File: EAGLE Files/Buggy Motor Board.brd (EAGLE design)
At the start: 100 x 80 mm, 53 parts, among them CON0 M025MM, CON1 M025MM, IC4 4050D, IC5 LP298XS, U1 MCP2551, X1 MICROSD, X2 5566-24, X3 5566-24, Y2 16MHZ

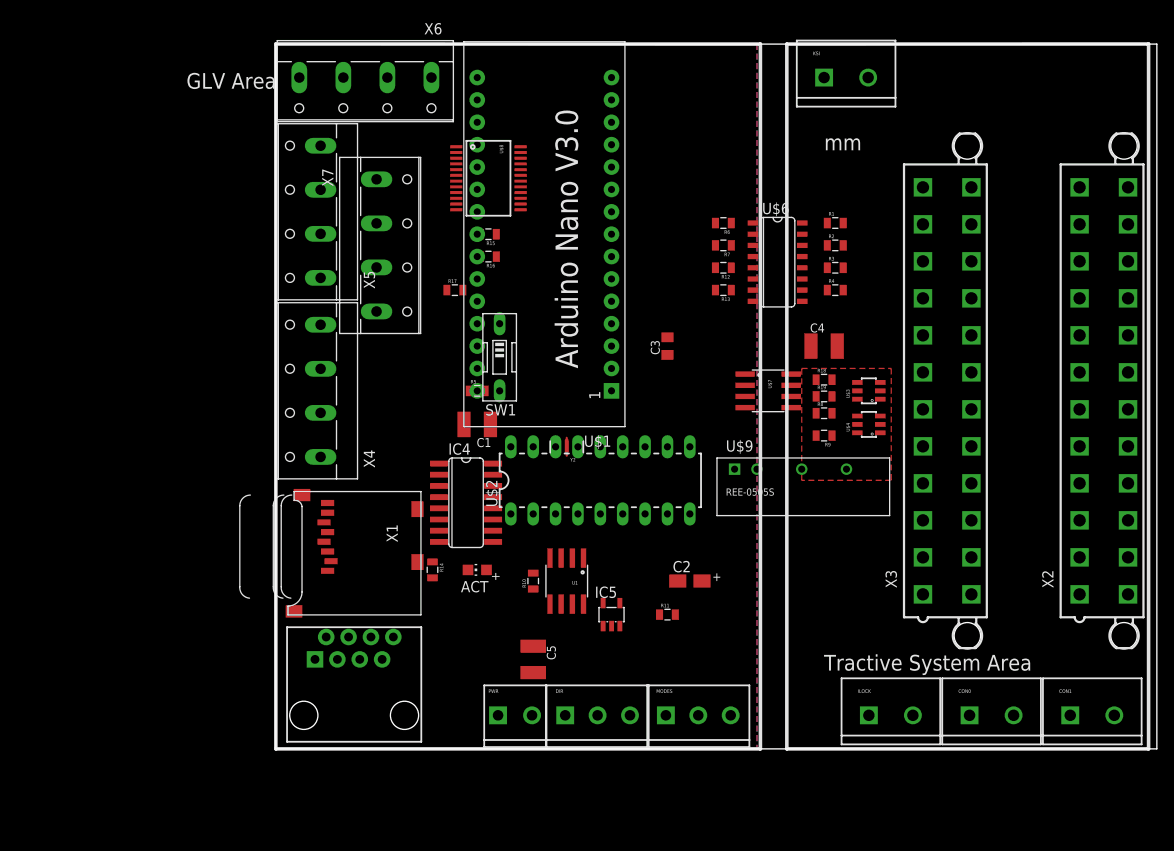
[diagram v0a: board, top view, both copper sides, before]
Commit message: Replace Nano with Teensy 3.1
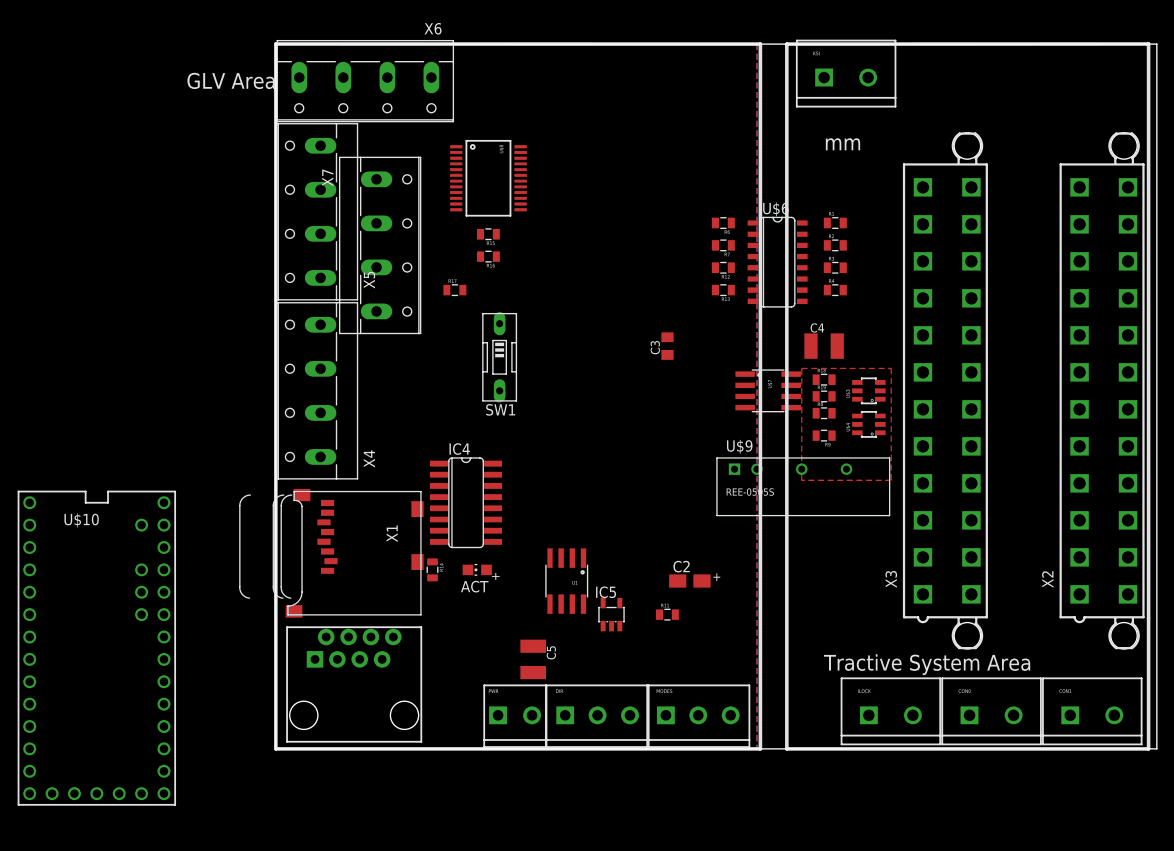
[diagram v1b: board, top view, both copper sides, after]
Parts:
- removed C1: (no value), rcl:C1210K
- removed R10, R5: (no value), SparkFun-Resistors:0805
- removed U$1: ARDUINO_NANO, Wetmelon-Boards:ARDUINO_NANO
- removed U$2: MCP2515, Wetmelon-DigitalIC:DIL18
- removed Y2: 16MHZ, SparkFun-FreqCtrl:RESONATOR-SMD
- added U$10: TEENSY_3.1+4, Teensy_3_Series_Board_v1.0:TEENSY_3.1+4
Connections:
- removed net CAN_CS: U$1.SS*, U$2.12
- removed net INT0: U$1.D2, U$2.16
- removed net INT1: U$1.D3*
- removed net N$1: U$1.3V3
- removed net N$10: U$2.17
- removed net N$11: U$2.18
- removed net N$14: U$2.7, Y2.1
- removed net N$2: U$2.8, Y2.3
- removed net N$23: R5.1, U$1.RES, U$1.RES@1
- removed net N$28: U$1.D8
- removed net N$3: R10.2, U$2.11
- removed net N$4: U$2.3
- removed net N$5: U$2.4
- removed net N$6: U$2.5
- removed net N$9: U$2.6
- new net +3.3V: U1.3
- new net 3.3V: U$10.3.3V, U$10.3.3V1
- new net AREF: U$10.AREF
- new net VBAT: U$10.VBAT
- new net VIN: U$10.VIN
- new net VUSB: U$10.VUSB
- net +12V: no longer C1.1, R5.2, U$1.VIN
- net +5V: no longer R10.1, U$1.+5V, U$2.10, U1.3
- net AGND: now also U$10.AGND
- net AMUX0: no longer U$1.A0
- net AMUX1: no longer U$1.A1
- net AMUX2: no longer U$1.A2
- net AMUX3: no longer U$1.A3
- net AMUX_IN: no longer U$1.A6
- net GND: now also U$10.GND, U$10.GND1; no longer C1.2, U$1.GND, U$1.GND@1, U$2.9, Y2.2
- net MISO: now also U$10.12; no longer U$1.MISO, U$2.13
- net MOSI: now also U$10.11; no longer U$1.MOSI*, U$2.14
- net RXCAN: now also U$10.4; no longer U$2.2
- net SCK: now also U$10.13; no longer U$1.SCK, U$2.15
- net SCL: now also U$10.19/A5; no longer U$1.SCL/A5
- net SDA: now also U$10.18/A4; no longer U$1.SDA/A4
- net SD_CS: no longer U$1.D9*
- net TXCAN: now also U$10.3; no longer U$2.1

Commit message: Add microfit connector
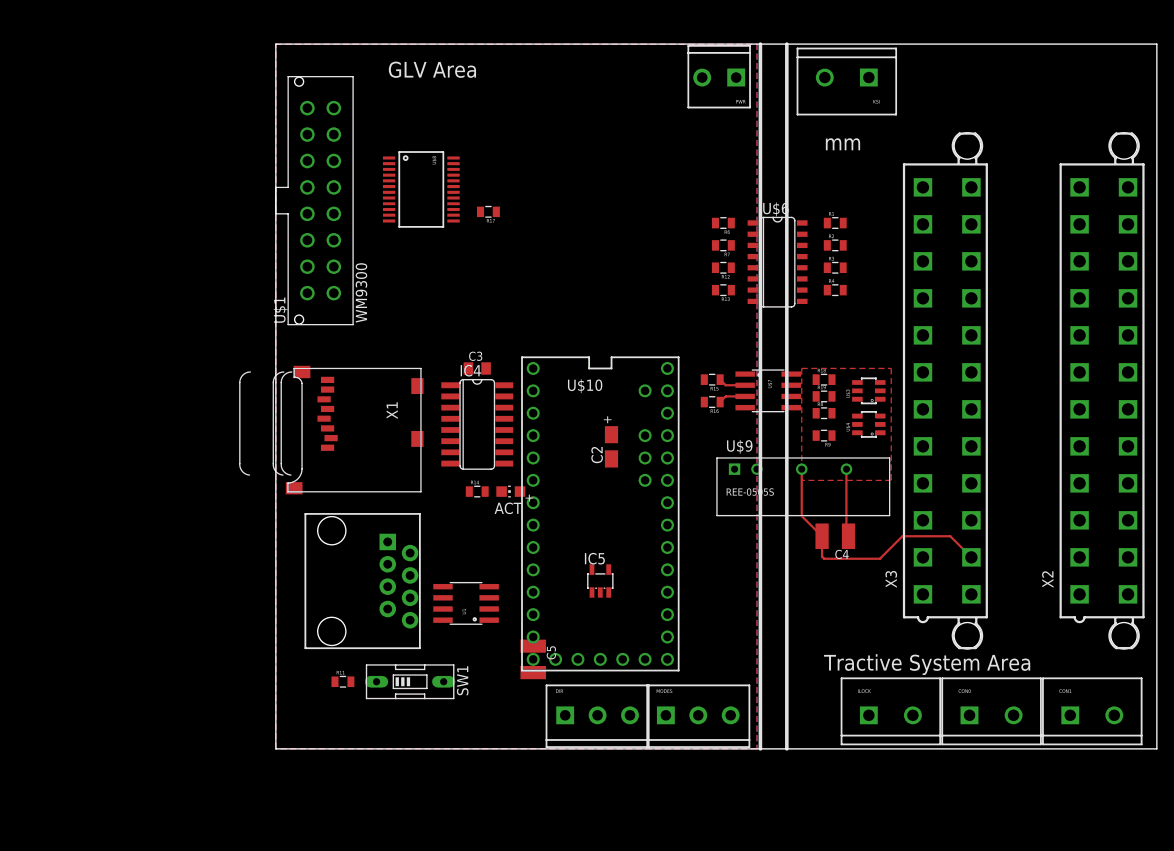
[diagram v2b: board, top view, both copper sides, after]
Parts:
- removed X4, X5, X6, X7: (no value), con-wago-500:W237-4
- added U$1: WM9300, Wetmelon-Connectors:WM9300
- moved PWR 77.1 mm to (52.1, 76.2), turned to 180 degrees
- moved U$10 59.1 mm to (36.8, 25.4)
- moved SW1 38.2 mm to (15.2, 7.62), turned to 270 degrees
- moved R11 37.6 mm to (7.62, 7.62)
- moved R15 30.3 mm to (49.5, 41.9)
- moved R16 30.3 mm to (49.5, 39.4)
- moved C3 21.7 mm to (22.9, 43.2), turned to 0 degrees
- moved C4 21.6 mm to (63.5, 24.1), turned to 180 degrees
- moved C2 17.6 mm to (38.1, 34.3), turned to 90 degrees
- moved U$5 15.5 mm to (6.35, 19.1), turned to 270 degrees
- moved X1 14.0 mm to (16.5, 43.2)
- moved U1 11.7 mm to (21.6, 16.5), turned to 90 degrees
- moved R14 10.2 mm to (22.9, 29.2), turned to 0 degrees
- moved ACT 9.67 mm to (26.7, 29.2)
- moved R17 9.67 mm to (24.1, 61.0), turned to 180 degrees
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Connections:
- removed net CLK: IC4.3, IC4.9
- new net N$1: U$10.2
- new net N$3: U$10.6
- new net N$4: U$10.7
- new net N$5: U$10.8
- net +5V: no longer U$8.24
- net AGND: now also KSI.2; no longer KSI.1
- net AMUX_IN: now also U$10.14/A0
- net CHAN0: now also U$1.8; no longer X4.1
- net CHAN1: now also U$1.7; no longer X4.2
- net CHAN10: now also U$1.11; no longer X6.3
- net CHAN11: now also U$1.12; no longer X6.4
- net CHAN12: now also U$1.13; no longer X7.1
- net CHAN13: now also U$1.14; no longer X7.2
- net CHAN14: now also U$1.15; no longer X7.3
- net CHAN15: now also U$1.16; no longer X7.4
- net CHAN2: now also U$1.6; no longer X4.3
- net CHAN3: now also U$1.5; no longer X4.4
- net CHAN4: now also U$1.4; no longer X5.1
- net CHAN5: now also U$1.3; no longer X5.2
- net CHAN6: now also U$1.2; no longer X5.3
- net CHAN7: now also U$1.1; no longer X5.4
- net CHAN8: now also U$1.9; no longer X6.1
- net CHAN9: now also U$1.10; no longer X6.2
- net KSI: now also KSI.1; no longer KSI.2
- net SCK: now also IC4.3, IC4.9
- net SD_CS: now also U$10.5
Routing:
- net GND1: track 0.00 -> 30.0 mm
- net +5V/1: track 0.00 -> 7.72 mm
- net SCL: track 0.00 -> 3.10 mm
- net SDA: track 0.00 -> 3.10 mm
- added copper zone on layer 1, net GND
- removed copper zone on layer 1, net +5V

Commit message: Tweaks
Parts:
- moved U$10 35.6 mm to (36.8, 61.0)
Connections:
- removed net 3.3V: U$10.3.3V, U$10.3.3V1
- removed net AREF: U$10.AREF
- removed net N$3: U$10.6
- removed net N$4: U$10.7
- removed net N$5: U$10.8
- net +3V3: now also R15.2, R16.2, U$10.3.3V, U$10.3.3V1, U$10.AREF, U$7.1
- net +5V: now also U$8.24; no longer R15.2, R16.2, U$7.1
- net AGND: no longer KSI.2, U$6.11, U$6.13, U$6.15, U$6.9
- net AMUX0: now also U$10.6
- net AMUX1: now also U$10.7
- net AMUX2: now also U$10.8
- net AMUX3: now also U$10.9
- net GND1: now also KSI.2, U$6.11, U$6.13, U$6.15, U$6.9
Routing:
- net AMUX1: track 0.00 -> 17.2 mm, vias 0 -> 1
- net AMUX0: track 0.00 -> 16.5 mm, vias 0 -> 1
- net AMUX3: track 0.00 -> 11.8 mm
- net AMUX2: track 0.00 -> 11.0 mm

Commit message: Pre-Share Update
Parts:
- removed U1: MCP2551, SparkFun-DigitalIC:SO08
- added C1: .33uF, rcl:C0805
- added C6: .1uF, rcl:C0805
- added IC1: (no value), SparkFun-PowerIC:78XXL
- added MCP-2562: MCP2562, Wetmelon-DigitalIC:SO08
- moved U$1 1.27 mm to (5.08, 63.5)
- moved U$9 1.27 mm to (50.8, 31.8)
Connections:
- removed net +3.3V: U1.3
- removed net N$1: U$10.2
- removed net VIN: U$10.VIN
- net +12V: now also C1.1, IC1.IN
- net +3V3: now also MCP-2562.5
- net +5V: now also C6.1, IC1.OUT, MCP-2562.3, U$10.VIN
- net AMUX_EN: now also U$10.10
- net CANH: now also MCP-2562.7; no longer U1.7
- net CANL: now also MCP-2562.6; no longer U1.6
- net GND: now also C1.2, C6.2, IC1.GND, MCP-2562.2, MCP-2562.8; no longer U1.2, U1.8
- net RXCAN: now also MCP-2562.4; no longer U1.4
- net TXCAN: now also MCP-2562.1; no longer U1.1
